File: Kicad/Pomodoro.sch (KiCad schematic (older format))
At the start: 37 parts, among them IC1 ATTINY48-MM, P1 CONN_02X03, Q1 FCX717TA, Q2 FCX717TA, Q3 FCX717TA, Q4 FCX717TA, SW1 SPST, SW2 SW_PUSH, U1 LM7805

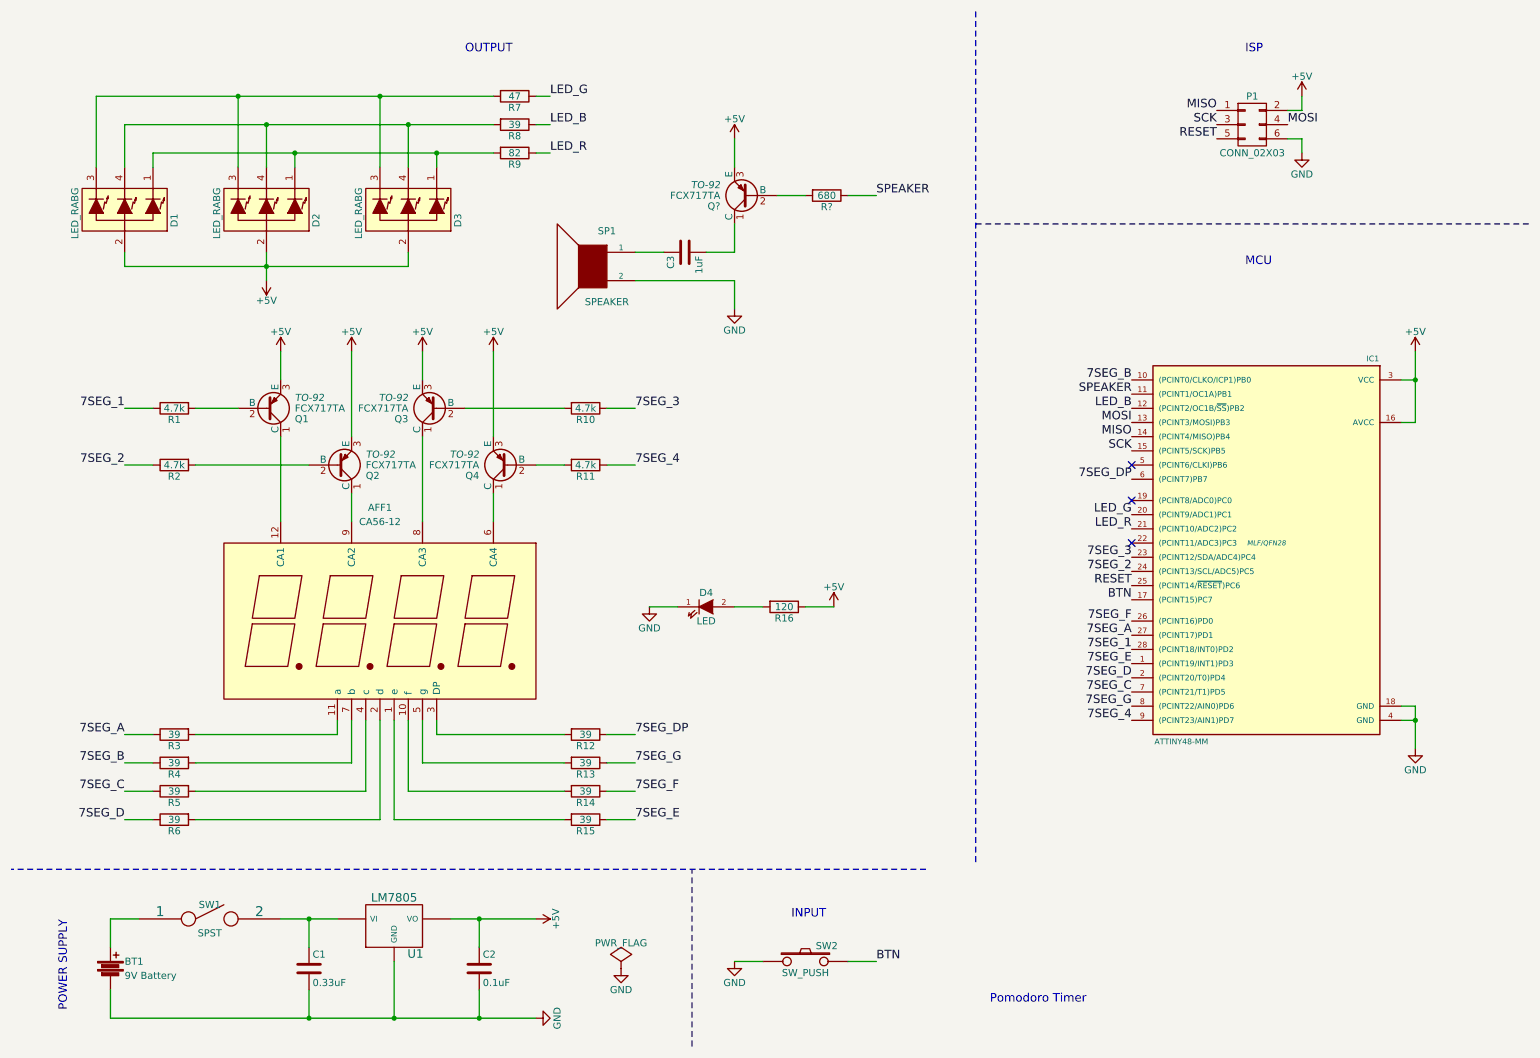
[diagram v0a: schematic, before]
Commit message: Updates the schema based on feedback
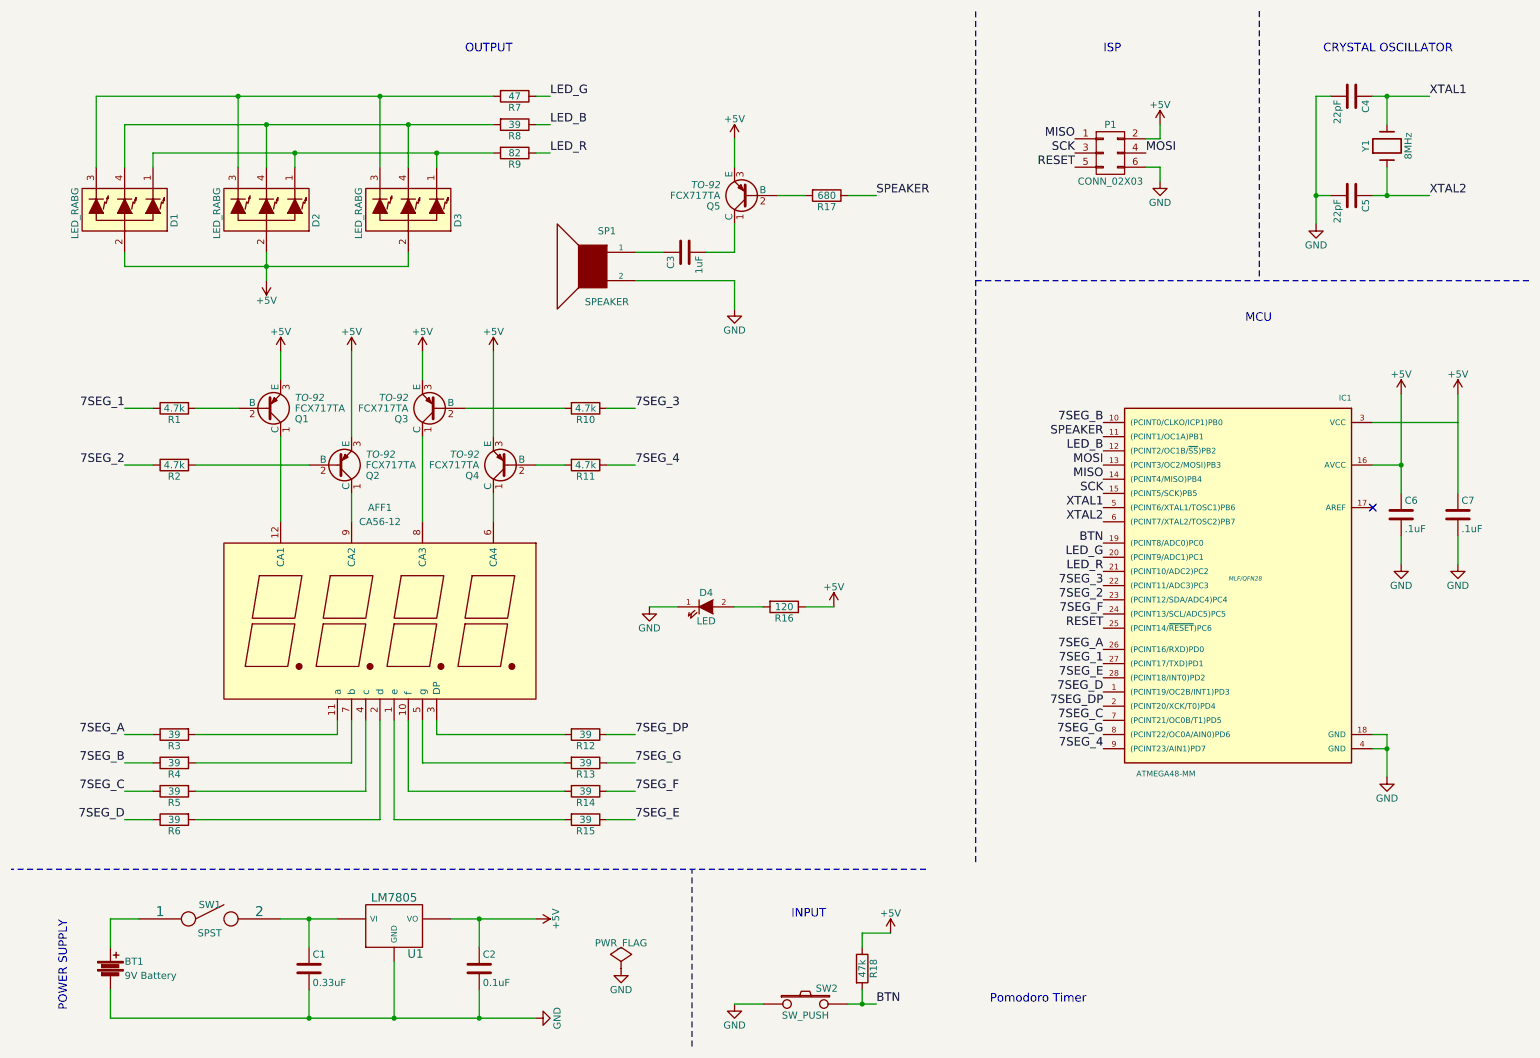
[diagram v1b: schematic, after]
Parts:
- removed IC1: ATTINY48-MM, MLF/QFN28, symbol ATTINY48-MM
- added C4, C5: 22pF, symbol C
- added C6, C7: .1uF, symbol C
- added IC1: ATMEGA48-MM, MLF/QFN28, symbol ATMEGA48-MM
- added R18: 47k, symbol R
- added Y1: 8MHz, symbol Crystal
- gave numbers to parts that had none: 2
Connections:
- net +5V: now also C6.1, C7.1, IC1.16 (AVCC), R18.1
- net 7SEG_1: now also IC1.27 ((PCINT17/TXD)PD1)
- net 7SEG_2: now also IC1.23 ((PCINT12/SDA/ADC4)PC4)
- net 7SEG_3: now also IC1.22 ((PCINT11/ADC3)PC3)
- net 7SEG_4: now also IC1.9 ((PCINT23/AIN1)PD7)
- net 7SEG_A: now also IC1.26 ((PCINT16/RXD)PD0)
- net 7SEG_B: now also IC1.10 ((PCINT0/CLKO/ICP1)PB0)
- net 7SEG_C: now also IC1.7 ((PCINT21/OC0B/T1)PD5)
- net 7SEG_D: now also IC1.1 ((PCINT19/OC2B/INT1)PD3)
- net 7SEG_DP: now also IC1.2 ((PCINT20/XCK/T0)PD4)
- net 7SEG_E: now also IC1.28 ((PCINT18/INT0)PD2)
- net 7SEG_F: now also IC1.24 ((PCINT13/SCL/ADC5)PC5)
- net 7SEG_G: now also IC1.8 ((PCINT22/OC0A/AIN0)PD6)
- net BTN: now also IC1.19 ((PCINT8/ADC0)PC0), R18.2
- net GND: now also C4.2, C5.2, C6.2, C7.2, IC1.18 (GND), IC1.4 (GND)
- net LED_B: now also IC1.12 ((PCINT2/OC1B/~SS~)PB2)
- net LED_G: now also IC1.20 ((PCINT9/ADC1)PC1)
- net LED_R: now also IC1.21 ((PCINT10/ADC2)PC2)
- net MISO: now also IC1.14 ((PCINT4/MISO)PB4)
- net MOSI: now also IC1.13 ((PCINT3/OC2/MOSI)PB3)
- net RESET: now also IC1.25 ((PCINT14/~RESET~)PC6)
- net SCK: now also IC1.15 ((PCINT5/SCK)PB5)
- net SPEAKER: now also IC1.11 ((PCINT1/OC1A)PB1)
- new net XTAL1: C4.1, IC1.5 ((PCINT6/XTAL1/TOSC1)PB6), Y1.2
- new net XTAL2: C5.1, IC1.6 ((PCINT7/XTAL2/TOSC2)PB7), Y1.1
- no-connect marks 3 -> 1
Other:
- note added: "CRYSTAL OSCILLATOR"
- moved on the sheet: P1, SW2
